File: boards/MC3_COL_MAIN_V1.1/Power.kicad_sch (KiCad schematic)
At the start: 34 parts, among them J1 SUPPLY_IN, Q1 AO4421, U1 AMS1117-3.3, U12 LM61460AANRJRR

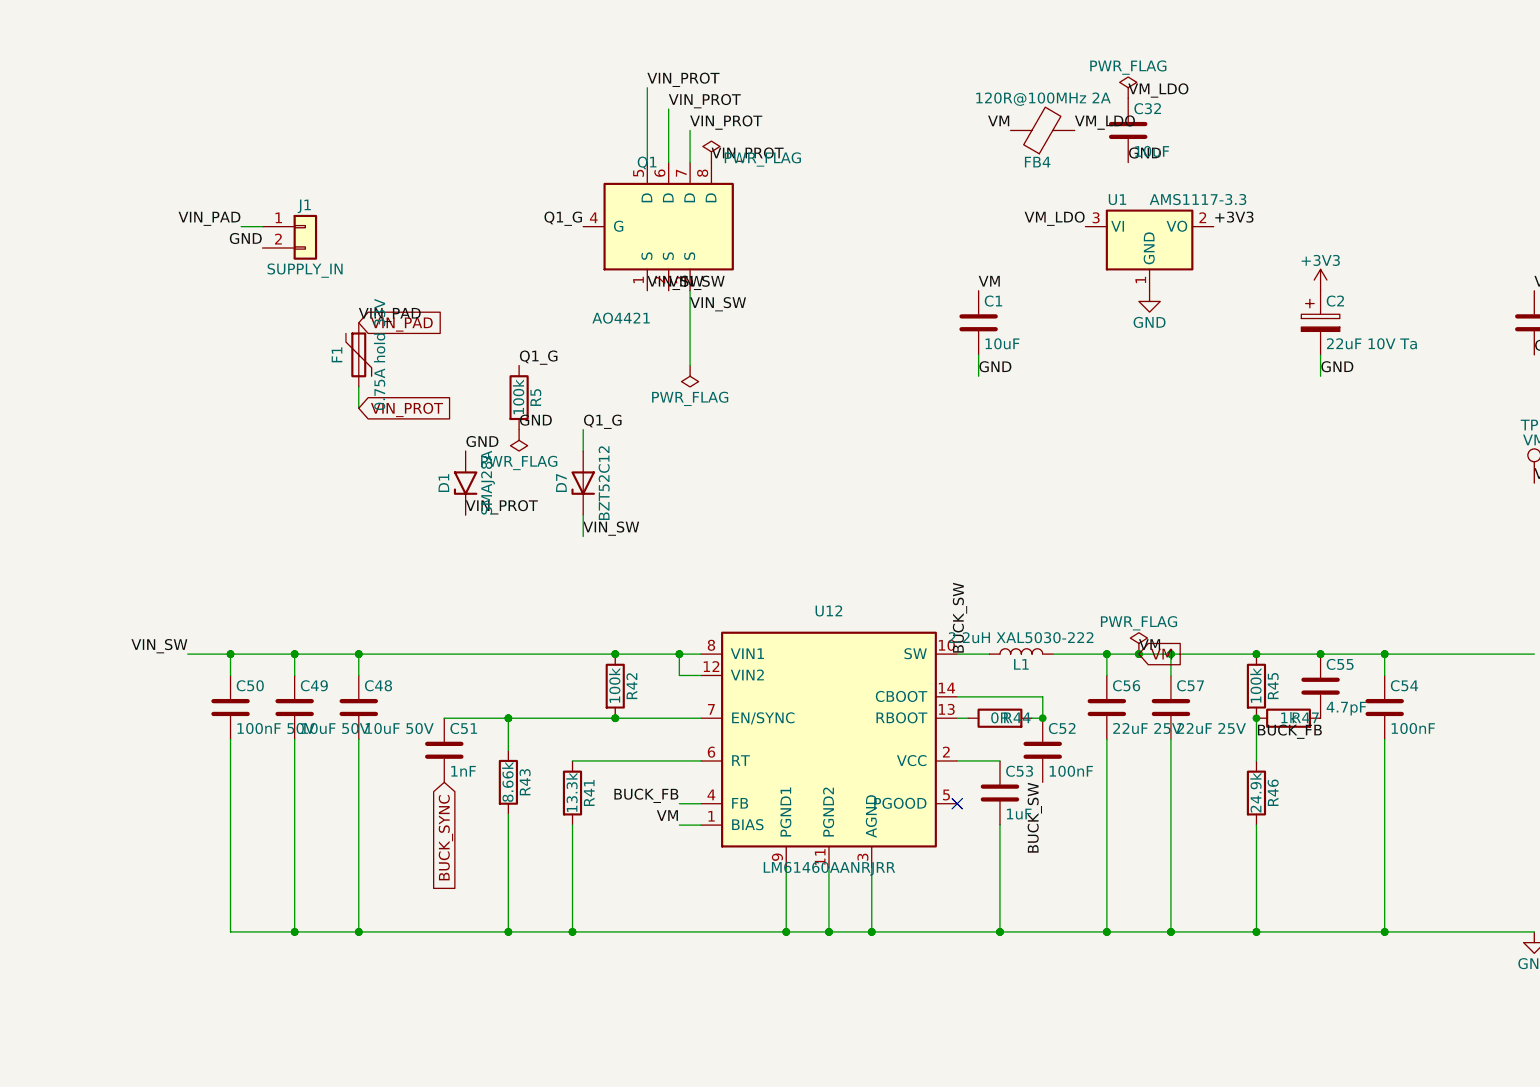
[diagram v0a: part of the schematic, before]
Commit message: V1.1 Power: named labels restored on BUCK_EN/RT/BOOT/VCC nodes
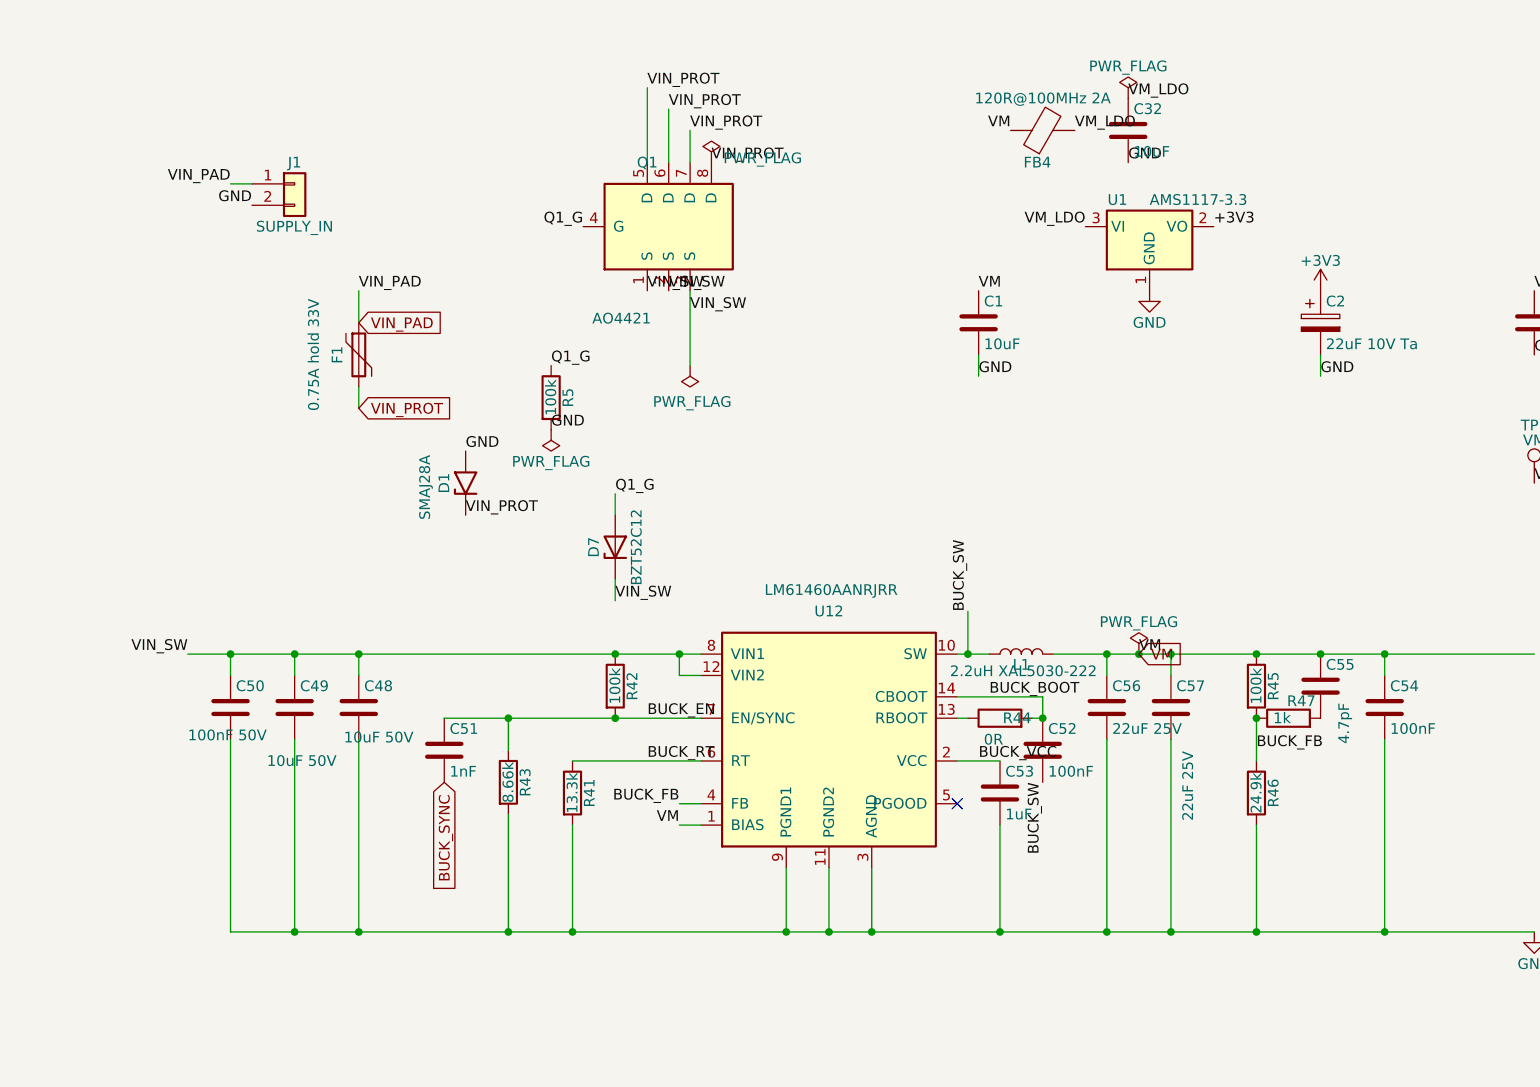
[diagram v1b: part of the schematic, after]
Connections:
- net BUCK_EN: now reaches C51.1, R42.2, R43.1, U12.7 (EN/SYNC)
- net BUCK_VCC: now reaches C53.1, U12.2 (VCC)
- net BUCK_BOOT: now reaches C52.1, R44.2, U12.14 (CBOOT)
- net BUCK_RT: now reaches R41.1, U12.6 (RT)
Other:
- moved on the sheet: D7, J1, R5
